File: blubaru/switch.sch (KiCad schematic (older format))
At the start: 1 part, among them J7 AUDIO_SWITCH

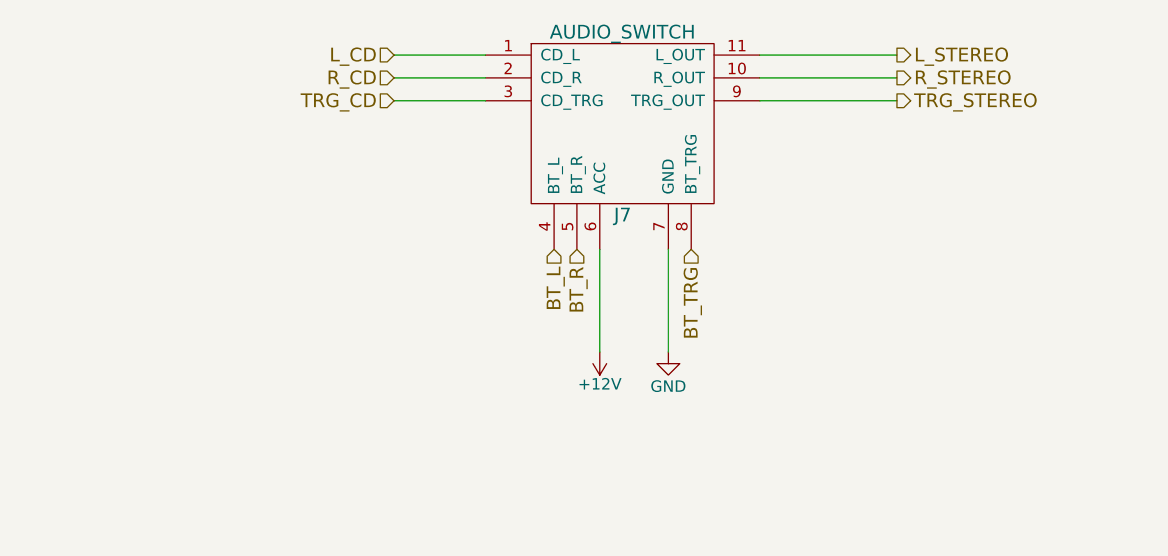
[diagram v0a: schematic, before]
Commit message: Put parts in the audio switch page.
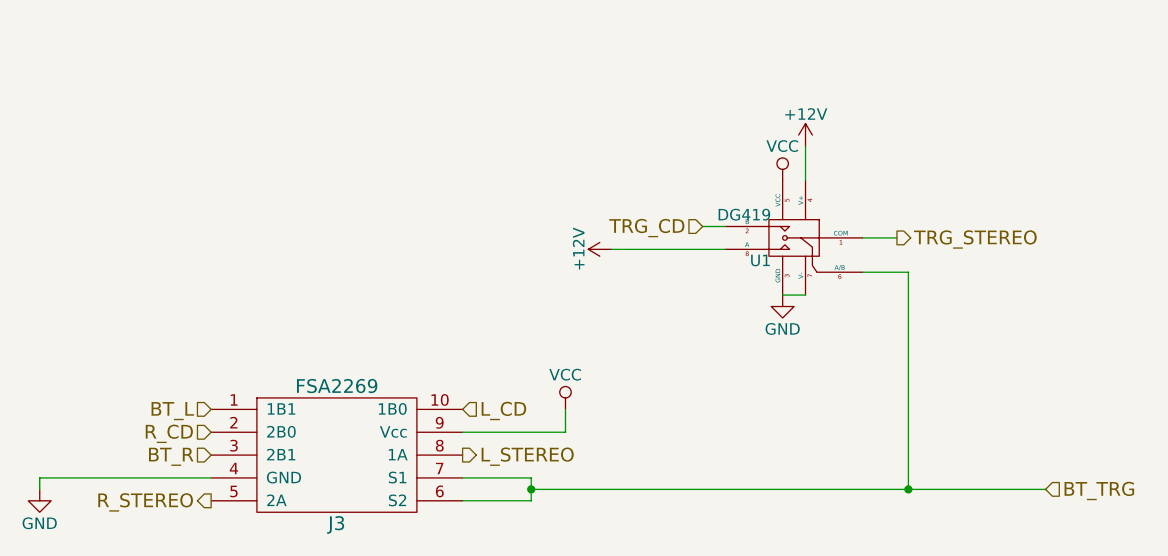
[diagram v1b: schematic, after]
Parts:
- removed J7: AUDIO_SWITCH, symbol AUDIO_SWITCH
- added J3: FSA2269, symbol FSA2269
- added U1: DG419, symbol DG419
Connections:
- net +12V: now also U1.4 (V+), U1.8 (A)
- net BT_L: now also J3.1 (1B1)
- net BT_R: now also J3.3 (2B1)
- net BT_TRG: now also J3.6 (S2), J3.7 (S1), U1.6 (A/B)
- net GND: now also J3.4 (GND), U1.3 (GND), U1.7 (V-)
- net L_CD: now also J3.10 (1B0)
- net L_STEREO: now also J3.8 (1A)
- net R_CD: now also J3.2 (2B0)
- net R_STEREO: now also J3.5 (2A)
- net TRG_CD: now also U1.2 (B)
- net TRG_STEREO: now also U1.1 (COM)
- new net VCC: J3.9 (Vcc), U1.5 (VCC)
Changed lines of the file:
@@
 Comment4 ""
 $EndDescr
+Wire Wire Line
+	6250 3600 6150 3600
+Wire Wire Line
+	6850 3650 7000 3650
+Text HLabel 5100 4400 2    60   Input ~ 0
+L_CD
+Text HLabel 4000 4500 0    60   Input ~ 0
+R_CD
+Text HLabel 6150 3600 0    60   Input ~ 0
+TRG_CD
+Text HLabel 4000 4400 0    60   Input ~ 0
+BT_L
+Text HLabel 4000 4600 0    60   Input ~ 0
+BT_R
+Text HLabel 7650 4750 2    60   Input ~ 0
+BT_TRG
+Text HLabel 5100 4600 2    60   Output ~ 0
+L_STEREO
+Text HLabel 4000 4800 0    60   Output ~ 0
+R_STEREO
+Text HLabel 7000 3650 2    60   Output ~ 0
+TRG_STEREO
 $Comp
-L AUDIO_SWITCH J7
-U 1 1 58A27F73
-P 5800 2750
-F 0 "J7" H 5800 1950 60  0000 C CNN
-F 1 "AUDIO_SWITCH" H 5800 2750 60  0000 C CNN
-F 2 "" H 5800 2750 60  0001 C CNN
-F 3 "" H 5800 2750 60  0001 C CNN
-	1    5800 2750
+L FSA2269 J3
+U 1 1 58B3B18B
+P 4550 4300
+F 0 "J3" H 4550 3700 60  0000 C CNN
+F 1 "FSA2269" H 4550 4300 60  0000 C CNN
+F 2 "" H 4550 4300 60  0001 C CNN
+F 3 "" H 4550 4300 60  0001 C CNN
+	1    4550 4300
+	1    0    0    -1
+$EndComp
+$Comp
+L GND #PWR05
+U 1 1 58B3B20A
+P 3250 4750
+F 0 "#PWR05" H 3250 4500 50  0001 C CNN
+F 1 "GND" H 3250 4600 50  0000 C CNN
+F 2 "" H 3250 4750 50  0000 C CNN
+F 3 "" H 3250 4750 50  0000 C CNN
+	1    3250 4750
 	1    0    0    -1
 $EndComp
 Wire Wire Line
-	5200 2850 4800 2850
+	4000 4700 3250 4700
 Wire Wire Line
-	5200 2950 4800 2950
-Wire Wire Line
-	5200 3050 4800 3050
-Wire Wire Line
-	6400 2850 7000 2850
-Wire Wire Line
-	6400 2950 7000 2950
-Wire Wire Line
-	6400 3050 7000 3050
-Wire Wire Line
-	6000 3700 6000 4150
+	3250 4700 3250 4750
 $Comp
-L GND #PWR05
-U 1 1 58A2DF5D
-P 6000 4150
-F 0 "#PWR05" H 6000 3900 50  0001 C CNN
-F 1 "GND" H 6000 4000 50  0000 C CNN
-F 2 "" H 6000 4150 50  0000 C CNN
-F 3 "" H 6000 4150 50  0000 C CNN
-	1    6000 4150
+L VCC #PWR06
+U 1 1 58B3B22E
+P 5550 4400
+F 0 "#PWR06" H 5550 4250 50  0001 C CNN
+F 1 "VCC" H 5550 4550 50  0000 C CNN
+F 2 "" H 5550 4400 50  0000 C CNN
+F 3 "" H 5550 4400 50  0000 C CNN
+	1    5550 4400
 	1    0    0    -1
 $EndComp
-Text HLabel 4800 2850 0    60   Input ~ 0
-L_CD
-Text HLabel 4800 2950 0    60   Input ~ 0
-R_CD
-Text HLabel 4800 3050 0    60   Input ~ 0
-TRG_CD
-Text HLabel 5500 3700 3    60   Input ~ 0
-BT_L
-Text HLabel 5600 3700 3    60   Input ~ 0
-BT_R
-Text HLabel 6100 3700 3    60   Input ~ 0
-BT_TRG
-Text HLabel 7000 2850 2    60   Output ~ 0
-L_STEREO
-Text HLabel 7000 2950 2    60   Output ~ 0
-R_STEREO
-Text HLabel 7000 3050 2    60   Output ~ 0
-TRG_STEREO
+Wire Wire Line
+	5100 4500 5550 4500
+Wire Wire Line
+	5550 4500 5550 4400
+Wire Wire Line
+	5400 4750 7050 4750
+Wire Wire Line
+	7050 4750 7650 4750
+Wire Wire Line
+	5100 4700 5400 4700
+Wire Wire Line
+	5400 4700 5400 4750
+Wire Wire Line
+	5400 4750 5400 4800
+Wire Wire Line
+	5400 4800 5100 4800
+Connection ~ 5400 4750
 $Comp
-L +12V #PWR06
-U 1 1 58B17E9C
-P 5700 4150
-F 0 "#PWR06" H 5700 4000 50  0001 C CNN
-F 1 "+12V" H 5700 4290 50  0000 C CNN
-F 2 "" H 5700 4150 50  0000 C CNN
-F 3 "" H 5700 4150 50  0000 C CNN
-	1    5700 4150
-	-1   0    0    1
+L DG419 U1
+U 1 1 58B47B5A
+P 6550 3650
+F 0 "U1" H 6650 3550 50  0000 L CNN
+F 1 "DG419" H 6650 3750 50  0000 L CNN
+F 2 "" H 6550 3650 60  0001 C CNN
+F 3 "" H 6550 3650 60  0001 C CNN
+	1    6550 3650
+	-1   0    0    -1
+$EndComp
+$Comp
+L GND #PWR07
+U 1 1 58B47DD4
+P 6500 3900
+F 0 "#PWR07" H 6500 3650 50  0001 C CNN
+F 1 "GND" H 6500 3750 50  0000 C CNN
+F 2 "" H 6500 3900 50  0000 C CNN
+F 3 "" H 6500 3900 50  0000 C CNN
+	1    6500 3900
+	1    0    0    -1
+$EndComp
+$Comp
+L +12V #PWR08
+U 1 1 58B47DEE
+P 6600 3250
+F 0 "#PWR08" H 6600 3100 50  0001 C CNN
+F 1 "+12V" H 6600 3390 50  0000 C CNN
+F 2 "" H 6600 3250 50  0000 C CNN
+F 3 "" H 6600 3250 50  0000 C CNN
+	1    6600 3250
+	1    0    0    -1
 $EndComp
 Wire Wire Line
-	5700 3700 5700 4150
+	6850 3800 7050 3800
+Wire Wire Line
+	7050 3800 7050 4750
+Connection ~ 7050 4750
+Wire Wire Line
+	6500 3900 6600 3900
+Wire Wire Line
+	6600 3250 6600 3400
+$Comp
+L VCC #PWR09
+U 1 1 58B483A9
+P 6500 3400
+F 0 "#PWR09" H 6500 3250 50  0001 C CNN
+F 1 "VCC" H 6500 3550 50  0000 C CNN
+F 2 "" H 6500 3400 50  0000 C CNN
+F 3 "" H 6500 3400 50  0000 C CNN
+	1    6500 3400
+	1    0    0    -1
+$EndComp
+$Comp
+L +12V #PWR?
+U 1 1 58B4A9F8
+P 5750 3700
+F 0 "#PWR?" H 5750 3550 50  0001 C CNN
+F 1 "+12V" H 5750 3840 50  0000 C CNN
+F 2 "" H 5750 3700 50  0000 C CNN
+F 3 "" H 5750 3700 50  0000 C CNN
+	1    5750 3700
+	0    -1   -1   0
+$EndComp
+Wire Wire Line
+	5750 3700 6250 3700
 $EndSCHEMATC

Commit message: Create footprints for breakout boards
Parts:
- U1: footprint (none) -> Housings_DIP:DIP-8_W7.62mm
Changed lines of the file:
@@
 encoding utf-8
 Sheet 4 8
-Title ""
-Date ""
+Title "Blubaru"
+Date "2017-02-28"
 Rev ""
 Comp ""
@@
 $EndComp
 $Comp
-L GND #PWR05
+L GND #PWR07
 U 1 1 58B3B20A
 P 3250 4750
-F 0 "#PWR05" H 3250 4500 50  0001 C CNN
+F 0 "#PWR07" H 3250 4500 50  0001 C CNN
 F 1 "GND" H 3250 4600 50  0000 C CNN
 F 2 "" H 3250 4750 50  0000 C CNN
@@
 	3250 4700 3250 4750
 $Comp
-L VCC #PWR06
+L VCC #PWR08
 U 1 1 58B3B22E
 P 5550 4400
-F 0 "#PWR06" H 5550 4250 50  0001 C CNN
+F 0 "#PWR08" H 5550 4250 50  0001 C CNN
 F 1 "VCC" H 5550 4550 50  0000 C CNN
 F 2 "" H 5550 4400 50  0000 C CNN
@@
 	5550 4500 5550 4400
 Wire Wire Line
-	5400 4750 7050 4750
-Wire Wire Line
-	7050 4750 7650 4750
+	5400 4750 7650 4750
 Wire Wire Line
 	5100 4700 5400 4700
 Wire Wire Line
-	5400 4700 5400 4750
-Wire Wire Line
-	5400 4750 5400 4800
+	5400 4700 5400 4800
 Wire Wire Line
 	5400 4800 5100 4800
@@
 F 0 "U1" H 6650 3550 50  0000 L CNN
 F 1 "DG419" H 6650 3750 50  0000 L CNN
-F 2 "" H 6550 3650 60  0001 C CNN
+F 2 "Housings_DIP:DIP-8_W7.62mm" H 6550 3650 60  0001 C CNN
 F 3 "" H 6550 3650 60  0001 C CNN
 	1    6550 3650
@@
 $EndComp
 $Comp
-L GND #PWR07
+L GND #PWR09
 U 1 1 58B47DD4
 P 6500 3900
-F 0 "#PWR07" H 6500 3650 50  0001 C CNN
+F 0 "#PWR09" H 6500 3650 50  0001 C CNN
 F 1 "GND" H 6500 3750 50  0000 C CNN
 F 2 "" H 6500 3900 50  0000 C CNN
@@
 $EndComp
 $Comp
-L +12V #PWR08
+L +12V #PWR010
 U 1 1 58B47DEE
 P 6600 3250
-F 0 "#PWR08" H 6600 3100 50  0001 C CNN
+F 0 "#PWR010" H 6600 3100 50  0001 C CNN
 F 1 "+12V" H 6600 3390 50  0000 C CNN
 F 2 "" H 6600 3250 50  0000 C CNN
@@
 	6600 3250 6600 3400
 $Comp
-L VCC #PWR09
+L VCC #PWR011
 U 1 1 58B483A9
 P 6500 3400
-F 0 "#PWR09" H 6500 3250 50  0001 C CNN
+F 0 "#PWR011" H 6500 3250 50  0001 C CNN
 F 1 "VCC" H 6500 3550 50  0000 C CNN
 F 2 "" H 6500 3400 50  0000 C CNN
@@
 $EndComp
 $Comp
-L +12V #PWR?
+L +12V #PWR012
 U 1 1 58B4A9F8
 P 5750 3700
-F 0 "#PWR?" H 5750 3550 50  0001 C CNN
+F 0 "#PWR012" H 5750 3550 50  0001 C CNN
 F 1 "+12V" H 5750 3840 50  0000 C CNN
 F 2 "" H 5750 3700 50  0000 C CNN

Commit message: Actually save the schematics that I had open.
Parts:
- J3: footprint (none) -> blubaru:FSA2269
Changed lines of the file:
@@
 F 0 "J3" H 4550 3700 60  0000 C CNN
 F 1 "FSA2269" H 4550 4300 60  0000 C CNN
-F 2 "" H 4550 4300 60  0001 C CNN
+F 2 "blubaru:FSA2269" H 4550 4300 60  0001 C CNN
 F 3 "" H 4550 4300 60  0001 C CNN
 	1    4550 4300
